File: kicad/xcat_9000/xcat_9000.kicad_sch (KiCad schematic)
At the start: 12 parts, among them IC1 SN65176BP, J1 Conn_02x14_Counter_Clockwise, J2 Pico, J3 Conn_02x03_Odd_Even, Q1 BSS138, U1 SN74LV244APWR, U2 SN74LV244APWR, U3 SN74LV244APWR

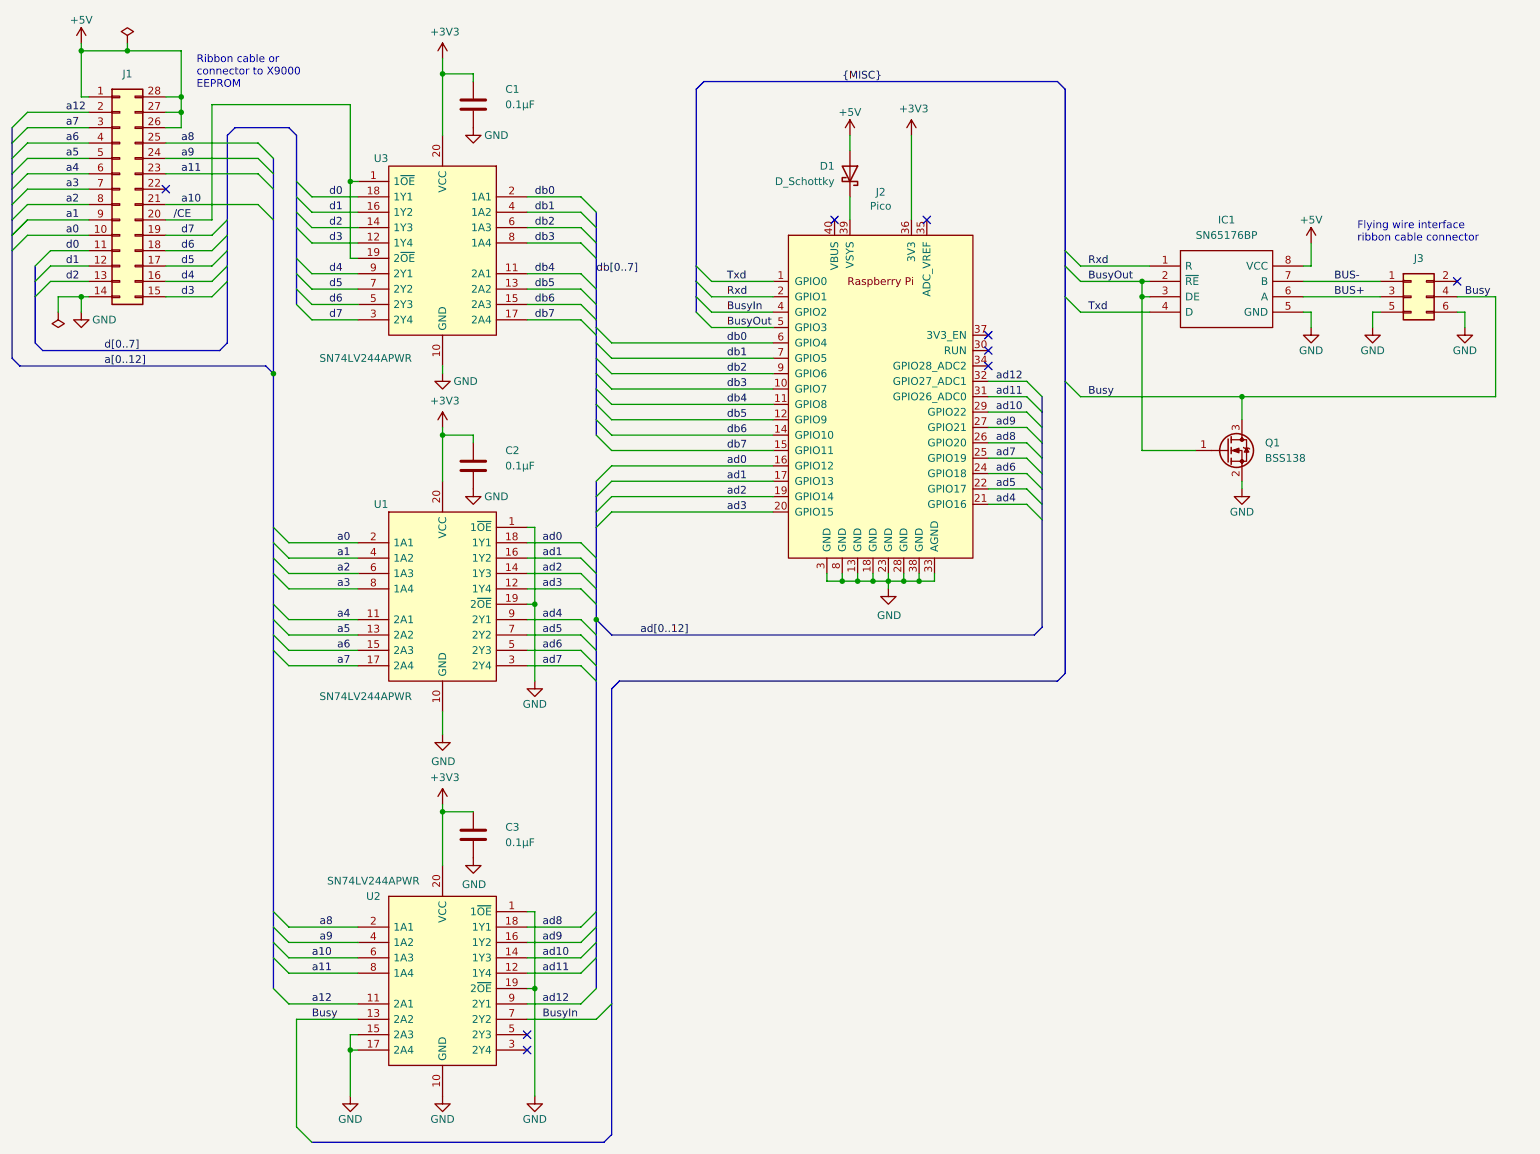
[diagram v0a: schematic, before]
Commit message: Xcat 9000 Rev B, multiplex a[0-7],adr[0,7], added CI-V, DH, I2C support.
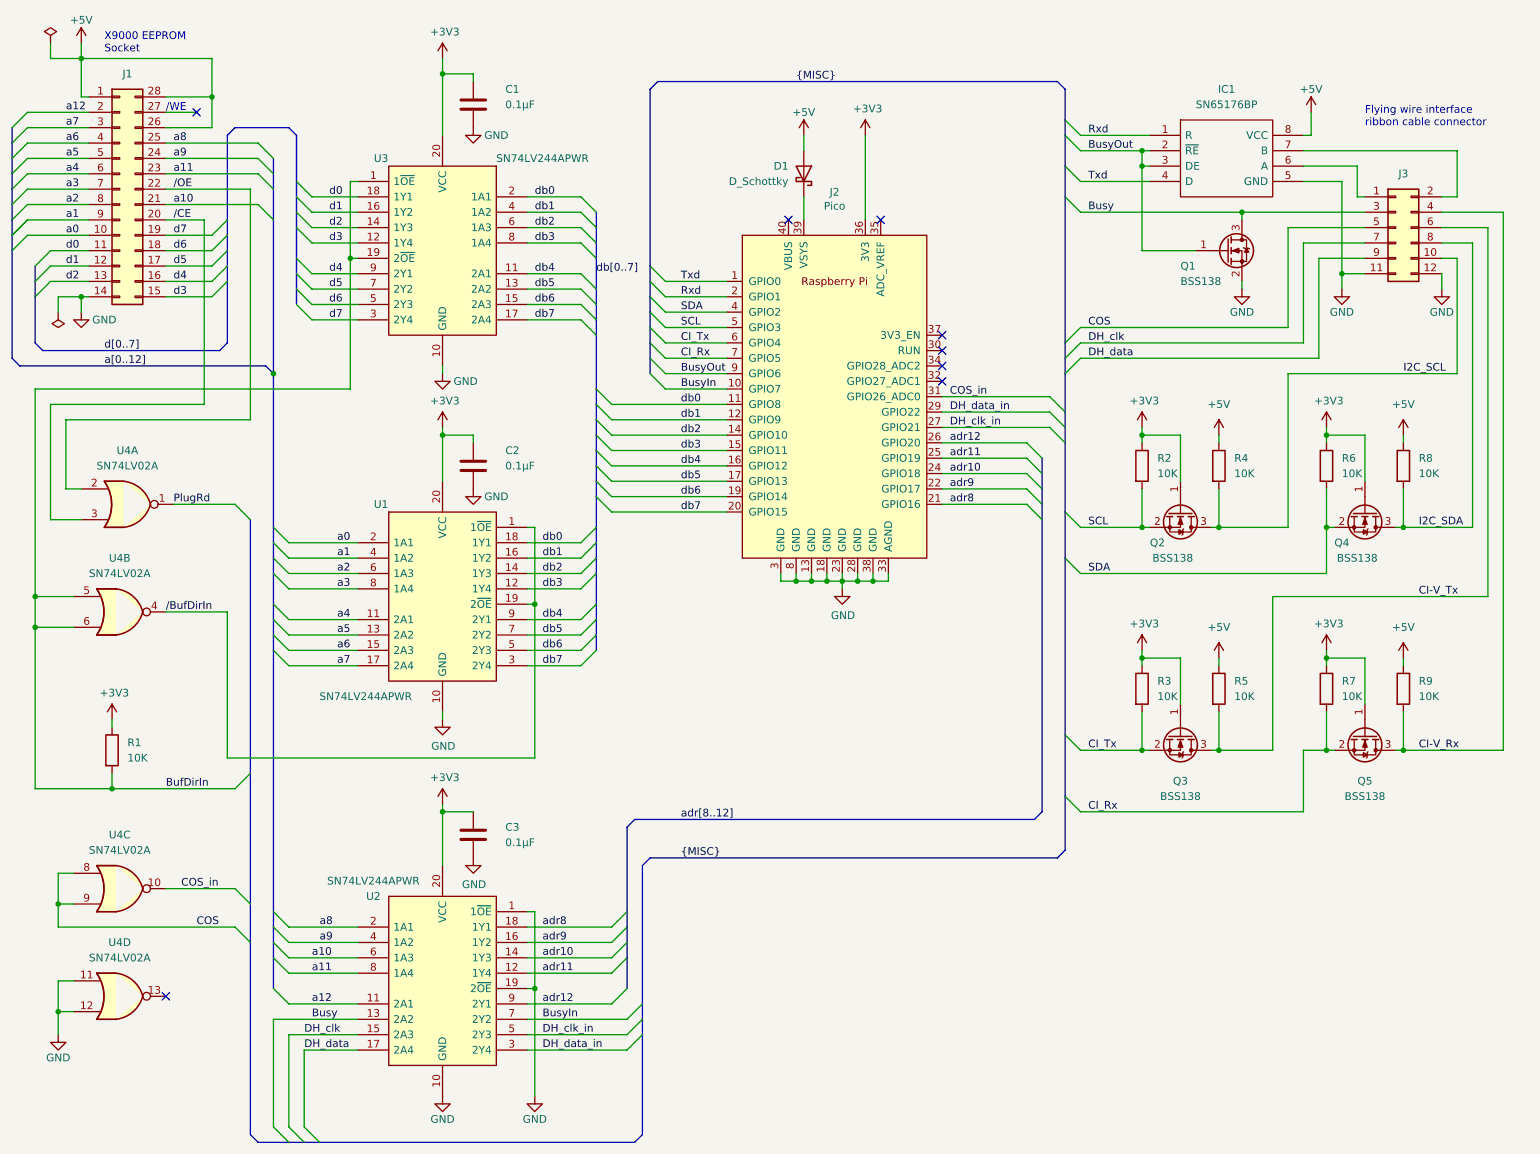
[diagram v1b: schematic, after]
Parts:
- removed J3: Conn_02x03_Odd_Even, symbol Connector_Generic:Conn_02x03_Odd_Even
- added J3: Conn_02x06_Odd_Even, symbol Connector_Generic:Conn_02x06_Odd_Even
- added Q2, Q3, Q4, Q5: BSS138, Package_TO_SOT_SMD:SOT-23, symbol Transistor_FET:BSS138
- added R1, R2, R3, R4, R5, R6, R7, R8, R9: 10K, symbol Device:R
- added U4: SN74LV02A, symbol 74xx:74HC02
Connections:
- net +3V3: now also Q2.1 (G), Q3.1 (G), Q4.1 (G), Q5.1 (G), R1.1, R2.1, R3.1, R6.1, R7.1
- net +5V: now also R4.1, R5.1, R8.1, R9.1; no longer J1.27 (Pin_27)
- net Busy: now also J3.3 (Pin_3)
- net BusyIn: now also J2.10 (GPIO7); no longer J2.4 (GPIO2)
- net BusyOut: now also J2.9 (GPIO6); no longer J2.5 (GPIO3)
- net GND: now also J3.11 (Pin_11), J3.12 (Pin_12), U4.11, U4.12; no longer U1.1 (1~{OE}), U1.19 (2~{OE}), U2.15 (2A3), U2.17 (2A4)
- net db0: now also J2.11 (GPIO8), U1.18 (1Y1); no longer J2.6 (GPIO4)
- net db1: now also J2.12 (GPIO9), U1.16 (1Y2); no longer J2.7 (GPIO5)
- net db2: now also J2.14 (GPIO10), U1.14 (1Y3); no longer J2.9 (GPIO6)
- net db3: now also J2.15 (GPIO11), U1.12 (1Y4); no longer J2.10 (GPIO7)
- net db4: now also J2.16 (GPIO12), U1.9 (2Y1); no longer J2.11 (GPIO8)
- net db5: now also J2.17 (GPIO13), U1.7 (2Y2); no longer J2.12 (GPIO9)
- net db6: now also J2.19 (GPIO14), U1.5 (2Y3); no longer J2.14 (GPIO10)
- net db7: now also J2.20 (GPIO15), U1.3 (2Y4); no longer J2.15 (GPIO11)
- net /CE: now also U4.3; no longer U3.1 (1~{OE}), U3.19 (2~{OE})
- net DH_data_in: now reaches U2.3 (2Y4)
- net DH_data_in: now also J2.29 (GPIO22)
- net DH_clk_in: now reaches U2.5 (2Y3)
- net DH_clk_in: now also J2.27 (GPIO21)
- net /OE: now reaches J1.22 (Pin_22)
- net /OE: now also U4.2
- net BUS+: no longer names the net of IC1.6 (A)
- net BUS+: now also J3.1 (Pin_1)
- net BUS-: no longer names the net of IC1.7 (B)
- net BUS-: now also J3.2 (Pin_2)
- removed net ad0: J2.16 (GPIO12), U1.18 (1Y1)
- removed net ad1: J2.17 (GPIO13), U1.16 (1Y2)
- net ad10 renamed adr10
- net adr10: now also J2.24 (GPIO18); no longer J2.29 (GPIO22)
- net ad11 renamed COS_in
- net COS_in: now also U4.10; no longer U2.12 (1Y4)
- net ad12: no longer names the net of J2.32 (GPIO27_ADC1)
- net ad12: no longer U2.9 (2Y1)
- removed net ad2: J2.19 (GPIO14), U1.14 (1Y3)
- removed net ad3: J2.20 (GPIO15), U1.12 (1Y4)
- net ad4 renamed adr8
- net adr8: now also U2.18 (1Y1); no longer U1.9 (2Y1)
- net ad5 renamed adr9
- net adr9: now also U2.16 (1Y2); no longer U1.7 (2Y2)
- removed net ad6: J2.24 (GPIO18), U1.5 (2Y3)
- net ad7 renamed adr11
- net adr11: now also U2.12 (1Y4); no longer U1.3 (2Y4)
- net ad8 renamed adr12
- net adr12: now also U2.9 (2Y1); no longer U2.18 (1Y1)
- removed net ad9: J2.27 (GPIO21), U2.16 (1Y2)
- new net BufDirIn: R1.2, U3.1 (1~{OE}), U3.19 (2~{OE}), U4.5, U4.6
- new net CI-V_Rx: J3.4 (Pin_4), Q5.3 (D), R9.2
- new net CI-V_Tx: J3.6 (Pin_6), Q3.3 (D), R5.2
- new net CI_Rx: J2.7 (GPIO5), Q5.2 (S), R7.2
- new net CI_Tx: J2.6 (GPIO4), Q3.2 (S), R3.2
- new net COS: J3.5 (Pin_5), U4.8, U4.9
- new net DH_clk: J3.7 (Pin_7), U2.15 (2A3)
- new net DH_data: J3.9 (Pin_9), U2.17 (2A4)
- new net I2C_SCL: J3.10 (Pin_10), Q2.3 (D), R4.2
- new net I2C_SDA: J3.8 (Pin_8), Q4.3 (D), R8.2
- new net PlugRd: U4.1
- new net SCL: J2.5 (GPIO3), Q2.2 (S), R2.2
- new net SDA: J2.4 (GPIO2), Q4.2 (S), R6.2
- new net /BufDirIn: U1.1 (1~{OE}), U1.19 (2~{OE}), U4.4
- no-connect marks 9 -> 8
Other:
- note added: "/WE"
- note added: "X9000 EEPROM Socket"
- note removed: "Ribbon cable or connector to X9000 EEPROM"
- moved on the sheet: D1, IC1, J2, Q1

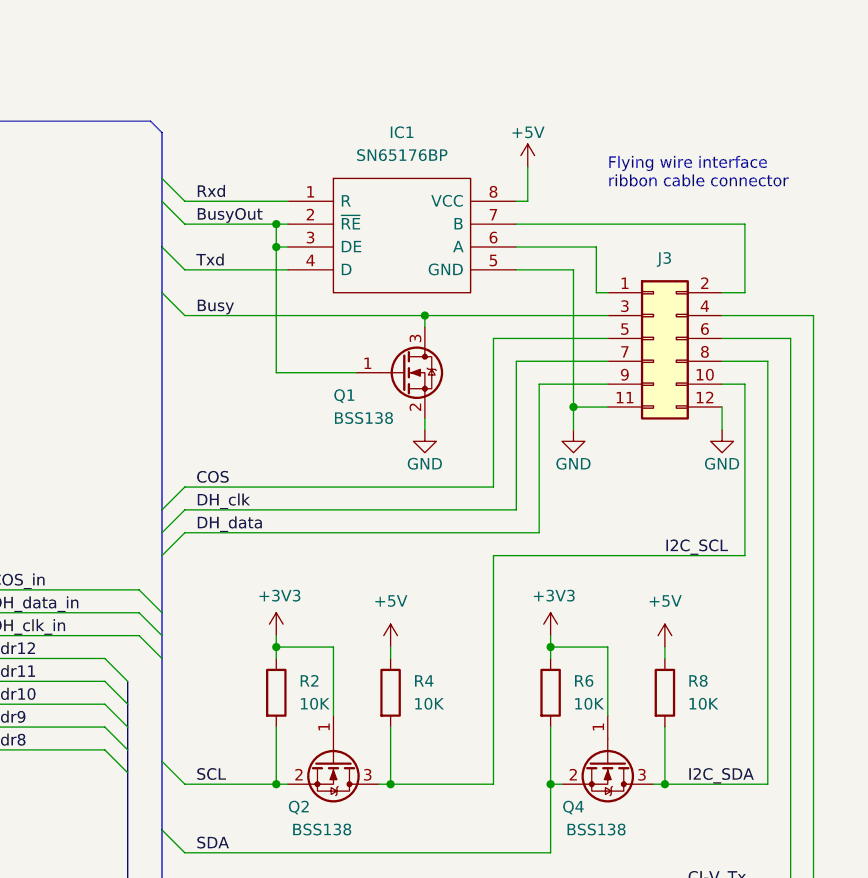
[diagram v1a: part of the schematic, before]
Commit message: Xcat 9000 Rev C: Added pullup resistors on DH interface.
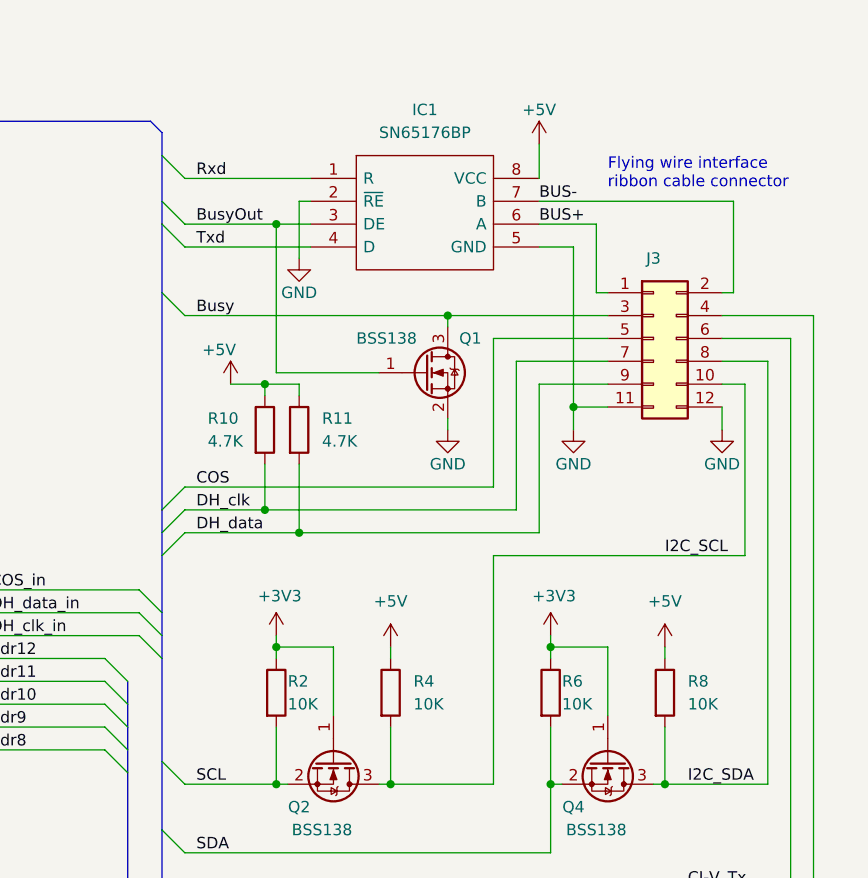
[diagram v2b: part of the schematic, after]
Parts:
- added R10, R11: 4.7K, symbol Device:R
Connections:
- net +5V: now also R10.1, R11.1
- net BusyOut: no longer IC1.2 (~{RE})
- net DH_clk: now also R10.2
- net DH_data: now also R11.2
- net GND: now also IC1.2 (~{RE})
- net BUS+: now reaches IC1.6 (A), J3.1 (Pin_1)
- net BUS-: now reaches IC1.7 (B), J3.2 (Pin_2)
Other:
- moved on the sheet: IC1, Q1

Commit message: Xcat 9000 Rev D: Connect PlugRd and BufDirIn to processor!
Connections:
- net BufDirIn: now also J2.34 (GPIO28_ADC2)
- net PlugRd: now also J2.32 (GPIO27_ADC1)
- no-connect marks 8 -> 6
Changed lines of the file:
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@@
   (title_block
     (title "Xcat 9000 code plug replacment for Syntor X9000")
-    (date "2022-08-26")
-    (rev "C")
+    (date "2022-08-29")
+    (rev "D")
     (company "Xcat group https://groups.io/g/xcat")
     (comment 2 "PCB: WA1JHK")
@@
   )
   (no_connect (at 170.18 66.04))
-  (no_connect (at 170.18 73.66))
   (no_connect (at 170.18 68.58))
-  (no_connect (at 170.18 71.12))
   (no_connect (at 41.91 175.26))
   (no_connect (at 160.02 46.99))
@@
     (stroke (width 0) (type default) (color 0 0 0 0))
   )
+  (bus_entry (at 190.5 76.2) (size -2.54 -2.54)
+    (stroke (width 0) (type default) (color 0 0 0 0))
+  )
   (bus_entry (at 186.69 88.9) (size -2.54 -2.54)
     (stroke (width 0) (type default) (color 0 0 0 0))
@@
     (stroke (width 0) (type default) (color 0 0 0 0))
   )
+  (bus_entry (at 190.5 73.66) (size -2.54 -2.54)
+    (stroke (width 0) (type default) (color 0 0 0 0))
+  )
   (bus_entry (at 186.69 93.98) (size -2.54 -2.54)
     (stroke (width 0) (type default) (color 0 0 0 0))
@@
     (stroke (width 0) (type default) (color 0 0 0 0))
   )
+  (wire (pts (xy 170.18 73.66) (xy 187.96 73.66))
+    (stroke (width 0) (type default) (color 0 0 0 0))
+  )
+  (wire (pts (xy 170.18 71.12) (xy 187.96 71.12))
+    (stroke (width 0) (type default) (color 0 0 0 0))
+  )
   (bus (pts (xy 113.03 50.8) (xy 113.03 53.34))
     (stroke (width 0) (type default) (color 0 0 0 0))
@@
     (stroke (width 0) (type default) (color 0 0 0 0))
   )
-  (bus (pts (xy 190.5 72.39) (xy 190.5 78.74))
+  (bus (pts (xy 190.5 72.39) (xy 190.5 73.66))
     (stroke (width 0) (type default) (color 0 0 0 0))
   )
@@
     (stroke (width 0) (type default) (color 0 0 0 0))
   )
+  (bus (pts (xy 190.5 76.2) (xy 190.5 78.74))
+    (stroke (width 0) (type default) (color 0 0 0 0))
+  )
   (wire (pts (xy 156.21 106.68) (xy 158.75 106.68))
     (stroke (width 0) (type default) (color 0 0 0 0))
@@
   )
   (wire (pts (xy 203.2 120.65) (xy 203.2 119.38))
+    (stroke (width 0) (type default) (color 0 0 0 0))
+  )
+  (bus (pts (xy 190.5 73.66) (xy 190.5 76.2))
     (stroke (width 0) (type default) (color 0 0 0 0))
   )
@@
     (effects (font (size 1.27 1.27)) (justify left bottom))
   )
+  (label "PlugRd" (at 171.45 73.66 0)
+    (effects (font (size 1.27 1.27)) (justify left bottom))
+  )
   (label "a6" (at 25.4 34.29 0)
     (effects (font (size 1.27 1.27)) (justify left bottom))
@@
   )
   (label "adr8" (at 104.14 163.83 0)
+    (effects (font (size 1.27 1.27)) (justify left bottom))
+  )
+  (label "CI-V_Rx" (at 254 45.72 0)
     (effects (font (size 1.27 1.27)) (justify left bottom))
   )
@@
     (effects (font (size 1.27 1.27)) (justify right bottom))
   )
+  (label "BufDirIn" (at 171.45 71.12 0)
+    (effects (font (size 1.27 1.27)) (justify left bottom))
+  )
   (label "a3" (at 72.39 107.95 180)
